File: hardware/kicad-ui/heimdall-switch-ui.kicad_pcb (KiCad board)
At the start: 2 copper layers, 26 x 13 mm, 3 parts, among them J1 B3B-XH-A, SW1 KSC641J

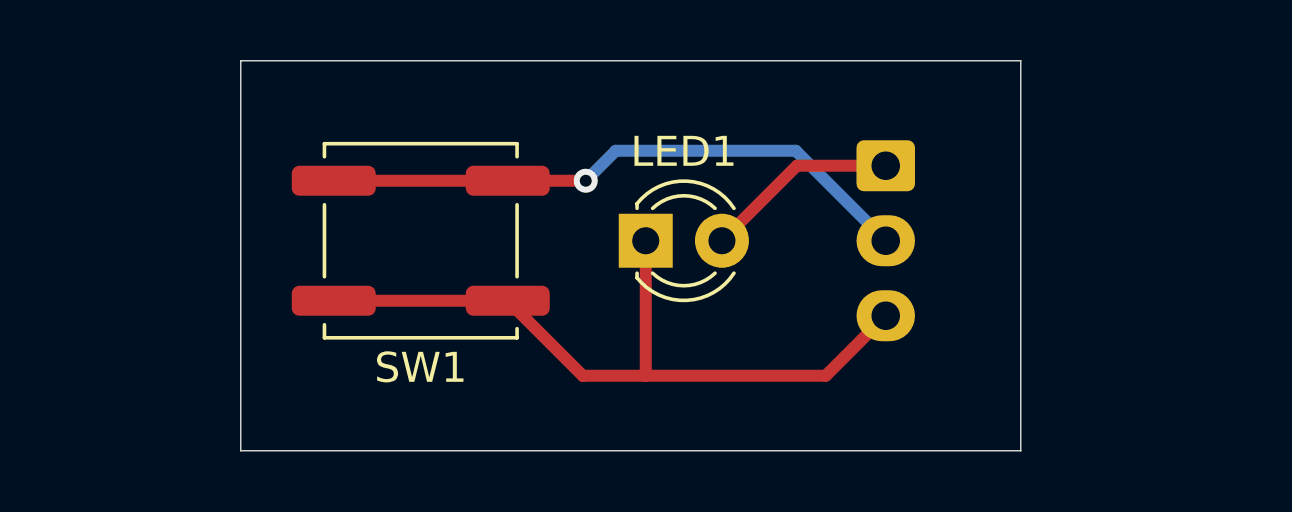
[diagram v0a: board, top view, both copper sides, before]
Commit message: UI daughter board: add two M3 mounting holes
Board grows to 39x13mm with M3 holes 32mm apart at the ends, for a
3D-printed housing on the outside of the hull (LED through the
housing, button sealed with an O-ring). ERC 0/0, DRC clean with
schematic parity.

Co-Authored-By: Claude Opus 5.5 <noreply@anthropic.com>
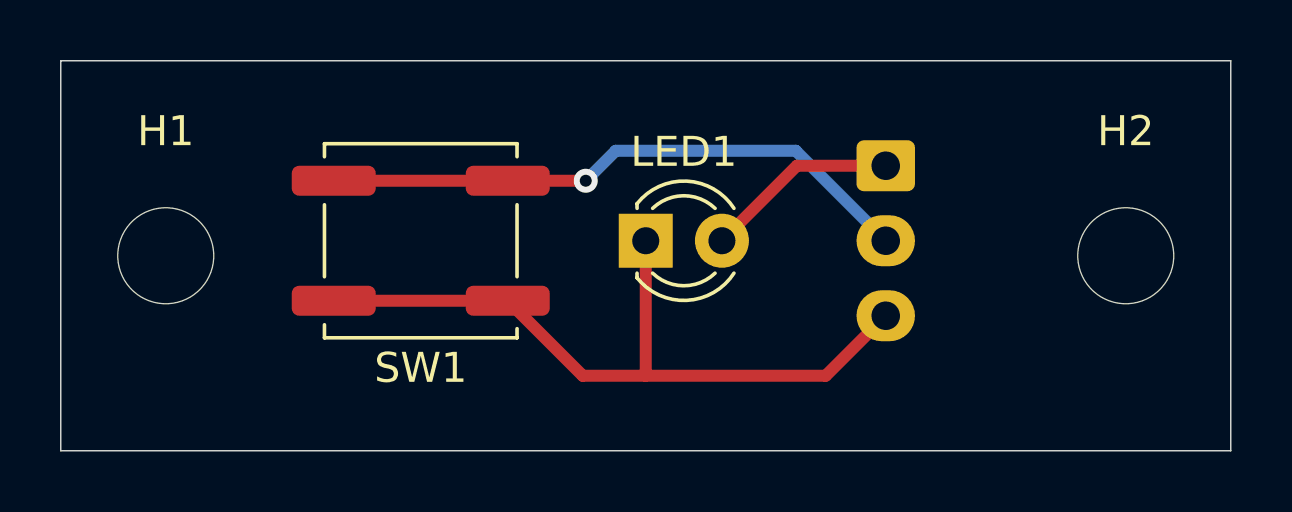
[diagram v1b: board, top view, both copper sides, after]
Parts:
- added H1: M3, MountingHole:MountingHole_3.2mm_M3, F.Cu at (97.5, 106.5)
- added H2: M3, MountingHole:MountingHole_3.2mm_M3, F.Cu at (129.5, 106.5)
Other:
- board size 26 x 13 mm -> 39 x 13 mm
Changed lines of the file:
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@@
 		)
+	)
+	(footprint "MountingHole:MountingHole_3.2mm_M3"
+		(layer "F.Cu")
+		(at 97.5 106.5)
+		(descr "Mounting Hole 3.2mm, M3, no annular, generated by kicad-footprint-generator mountinghole.py")
+		(tags "mountinghole M3")
+		(property "Reference" "H1"
+			(at 0 -4.15 0)
+			(layer "F.SilkS")
+			(effects
+				(font
+					(size 1 1)
+					(thickness 0.15)
+				)
+			)
+		)
+		(property "Value" "M3"
+			(at 0 4.15 0)
+			(layer "F.Fab")
+			(effects
+				(font
+					(size 1 1)
+					(thickness 0.15)
+				)
+			)
+		)
+		(property "Datasheet" ""
+			(at 0 0 0)
+			(layer "F.Fab")
+			(hide yes)
+			(effects
+				(font
+					(size 1.27 1.27)
+				)
+			)
+		)
+		(property "Description" ""
+			(at 0 0 0)
+			(layer "F.Fab")
+			(hide yes)
+			(effects
+				(font
+					(size 1.27 1.27)
+				)
+			)
+		)
+		(property "KiLib_Generator" "mounting_hardware/mounting_hole"
+			(at 0 0 0)
+			(layer "F.SilkS")
+			(hide yes)
+			(effects
+				(font
+					(size 1 1)
+					(thickness 0.15)
+				)
+			)
+		)
+		(sheetname "/")
+		(sheetfile "heimdall-switch-ui.kicad_sch")
+		(attr exclude_from_pos_files exclude_from_bom)
+		(duplicate_pad_numbers_are_jumpers no)
+		(fp_circle
+			(center 0 0)
+			(end 3.2 0)
+			(stroke
+				(width 0.15)
+				(type solid)
+			)
+			(fill no)
+			(layer "Cmts.User")
+		)
+		(fp_circle
+			(center 0 0)
+			(end 3.45 0)
+			(stroke
+				(width 0.05)
+				(type solid)
+			)
+			(fill no)
+			(layer "F.CrtYd")
+		)
+		(fp_text user "${REFERENCE}"
+			(at 0 0 0)
+			(layer "F.Fab")
+			(effects
+				(font
+					(size 1 1)
+					(thickness 0.15)
+				)
+			)
+		)
+		(pad "" np_thru_hole circle
+			(at 0 0)
+			(size 3.2 3.2)
+			(drill 3.2)
+			(layers "*.Cu" "*.Mask")
+		)
+		(embedded_fonts no)
 	)
 	(footprint "Button_Switch_SMD:SW_Push_1P1T_NO_CK_KSC6xxJ"
@@
 			)
 		)
+	)
+	(footprint "MountingHole:MountingHole_3.2mm_M3"
+		(layer "F.Cu")
+		(at 129.5 106.5)
+		(descr "Mounting Hole 3.2mm, M3, no annular, generated by kicad-footprint-generator mountinghole.py")
+		(tags "mountinghole M3")
+		(property "Reference" "H2"
+			(at 0 -4.15 0)
+			(layer "F.SilkS")
+			(effects
+				(font
+					(size 1 1)
+					(thickness 0.15)
+				)
+			)
+		)
+		(property "Value" "M3"
+			(at 0 4.15 0)
+			(layer "F.Fab")
+			(effects
+				(font
+					(size 1 1)
+					(thickness 0.15)
+				)
+			)
+		)
+		(property "Datasheet" ""
+			(at 0 0 0)
+			(layer "F.Fab")
+			(hide yes)
+			(effects
+				(font
+					(size 1.27 1.27)
+				)
+			)
+		)
+		(property "Description" ""
+			(at 0 0 0)
+			(layer "F.Fab")
+			(hide yes)
+			(effects
+				(font
+					(size 1.27 1.27)
+				)
+			)
+		)
+		(property "KiLib_Generator" "mounting_hardware/mounting_hole"
+			(at 0 0 0)
+			(layer "F.SilkS")
+			(hide yes)
+			(effects
+				(font
+					(size 1 1)
+					(thickness 0.15)
+				)
+			)
+		)
+		(sheetname "/")
+		(sheetfile "heimdall-switch-ui.kicad_sch")
+		(attr exclude_from_pos_files exclude_from_bom)
+		(duplicate_pad_numbers_are_jumpers no)
+		(fp_circle
+			(center 0 0)
+			(end 3.2 0)
+			(stroke
+				(width 0.15)
+				(type solid)
+			)
+			(fill no)
+			(layer "Cmts.User")
+		)
+		(fp_circle
+			(center 0 0)
+			(end 3.45 0)
+			(stroke
+				(width 0.05)
+				(type solid)
+			)
+			(fill no)
+			(layer "F.CrtYd")
+		)
+		(fp_text user "${REFERENCE}"
+			(at 0 0 0)
+			(layer "F.Fab")
+			(effects
+				(font
+					(size 1 1)
+					(thickness 0.15)
+				)
+			)
+		)
+		(pad "" np_thru_hole circle
+			(at 0 0)
+			(size 3.2 3.2)
+			(drill 3.2)
+			(layers "*.Cu" "*.Mask")
+		)
+		(embedded_fonts no)
 	)
 	(footprint "Connector_JST:JST_XH_B3B-XH-A_1x03_P2.50mm_Vertical"
@@
 	)
 	(gr_rect
-		(start 100 100)
-		(end 126 113)
+		(start 94 100)
+		(end 133 113)
 		(stroke
 			(width 0.05)
@@
 	)
 	(segment
+		(start 111.5 104)
+		(end 108.9 104)
+		(width 0.4)
+		(layer "F.Cu")
+		(net "/BTN")
+	)
+	(segment
 		(start 103.1 104)
-		(end 108.9 104)
-		(width 0.4)
-		(layer "F.Cu")
-		(net "/BTN")
-	)
-	(segment
-		(start 111.5 104)
 		(end 108.9 104)
 		(width 0.4)
@@
 	)
 	(segment
+		(start 118.5 103)
+		(end 112.5 103)
+		(width 0.4)
+		(layer "B.Cu")
+		(net "/BTN")
+	)
+	(segment
 		(start 112.5 103)
 		(end 111.5 104)
@@
 	)
 	(segment
-		(start 118.5 103)
-		(end 112.5 103)
-		(width 0.4)
-		(layer "B.Cu")
-		(net "/BTN")
+		(start 113.5 106)
+		(end 113.5 110.5)
+		(width 0.4)
+		(layer "F.Cu")
+		(net "GND")
+	)
+	(segment
+		(start 121.5 108.5)
+		(end 119.5 110.5)
+		(width 0.4)
+		(layer "F.Cu")
+		(net "GND")
+	)
+	(segment
+		(start 119.5 110.5)
+		(end 111.4 110.5)
+		(width 0.4)
+		(layer "F.Cu")
+		(net "GND")
 	)
 	(segment
@@
 	)
 	(segment
-		(start 113.5 106)
-		(end 113.5 110.5)
-		(width 0.4)
-		(layer "F.Cu")
-		(net "GND")
-	)
-	(segment
-		(start 119.5 110.5)
-		(end 111.4 110.5)
-		(width 0.4)
-		(layer "F.Cu")
-		(net "GND")
-	)
-	(segment
 		(start 111.4 110.5)
 		(end 108.9 108)
 		(width 0.4)
 		(layer "F.Cu")
-		(net "GND")
-	)
-	(segment
-		(start 121.5 108.5)
-		(end 119.5 110.5)
-		(width 0.4)
-		(layer "F.Cu")

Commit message: UI daughter board: tapped M3 holes, board down to 35x13mm
Holes are now 2.5mm M3 tap drill (screws thread into the board from
the housing), so only thread clearance is needed instead of a
head/washer keep-out. Project-local footprint
MountingHole_2.5mm_M3_Tapped. Holes 28.5mm apart. ERC 0/0, DRC clean
with schematic parity.

Co-Authored-By: Claude Opus 5.5 <noreply@anthropic.com>
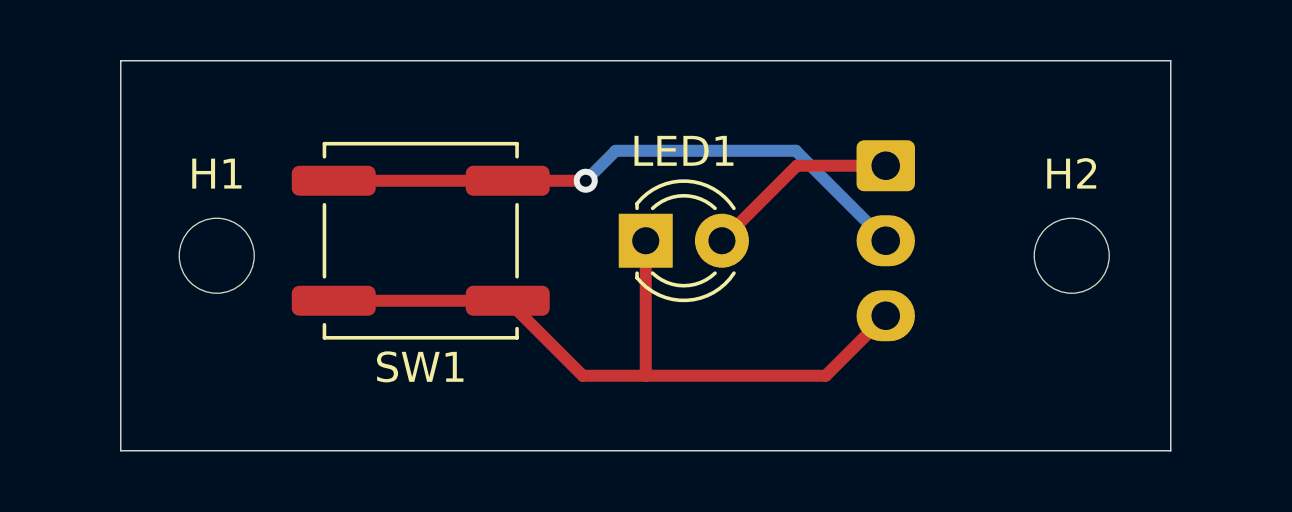
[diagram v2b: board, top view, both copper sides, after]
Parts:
- H1, H2: footprint MountingHole:MountingHole_3.2mm_M3 -> heimdall-switch-ui:MountingHole_2.5mm_M3_Tapped
- moved H2 1.80 mm to (127.7, 106.5)
- moved H1 1.70 mm to (99.2, 106.5)
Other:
- board size 39 x 13 mm -> 35 x 13 mm
